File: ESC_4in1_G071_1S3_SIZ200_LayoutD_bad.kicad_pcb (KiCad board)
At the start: 4 copper layers, 26 x 27 mm, 176 parts, among them J1 Conn_01x08, U1 STM32G071GBU6, U10 NCP81161MNTBG, U11 SIZ200DT-T1-GE3, U12 NCP81161MNTBG, U13 SIZ200DT-T1-GE3, U14 TPS630701, U15 TPS72733DSE, U16 INA185, U17 STM32G071GBU6, U18 NCP81161MNTBG, U19 SIZ200DT-T1-GE3, U2 NCP81161MNTBG, U20 NCP81161MNTBG, U21 STM32G071GBU6, U22 SIZ200DT-T1-GE3, U23 NCP81161MNTBG, U24 SIZ200DT-T1-GE3, U25 NCP81161MNTBG, U26 SIZ200DT-T1-GE3, U27 NCP81161MNTBG, U28 STM32G071GBU6, U29 SIZ200DT-T1-GE3, U3 SIZ200DT-T1-GE3, U30 NCP81161MNTBG, U31 SIZ200DT-T1-GE3, U4 NCP81161MNTBG, U5 SIZ200DT-T1-GE3, U6 NCP81161MNTBG, U7 SIZ200DT-T1-GE3, U8 NCP81161MNTBG, U9 SIZ200DT-T1-GE3

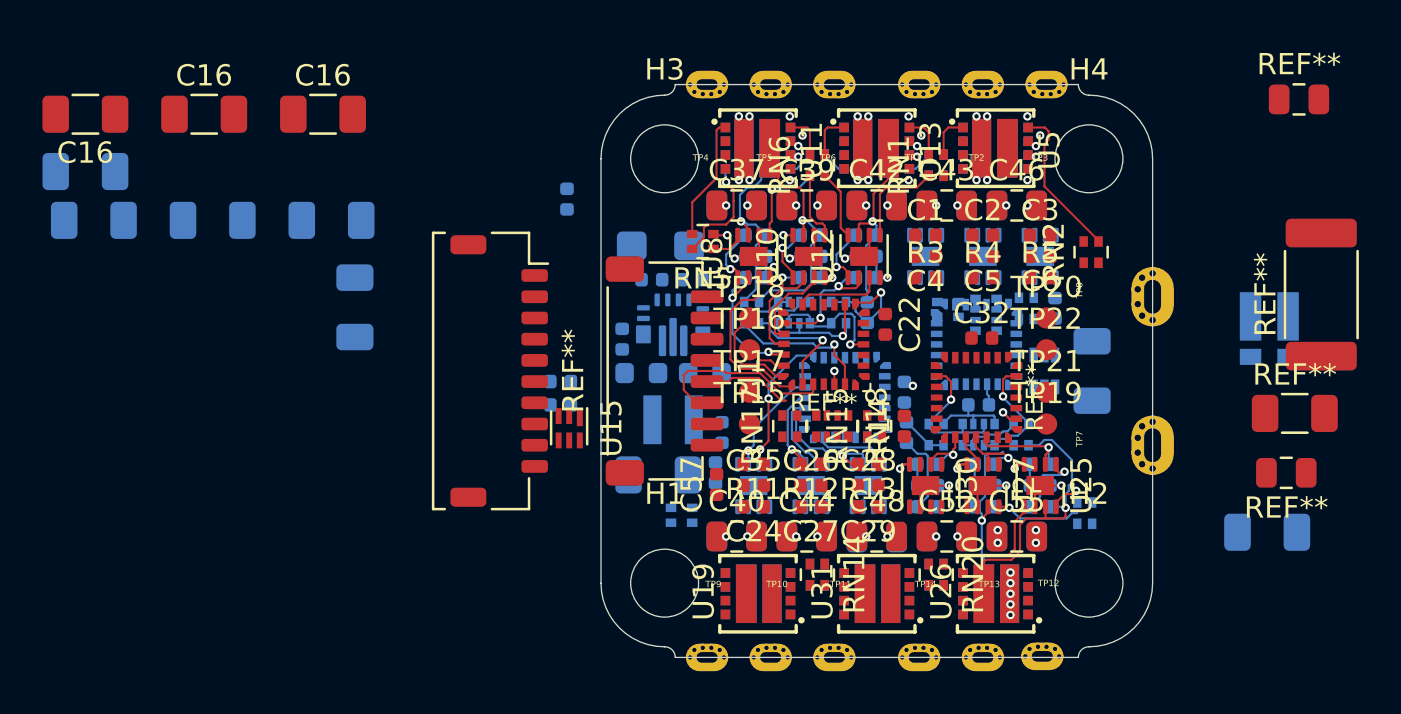
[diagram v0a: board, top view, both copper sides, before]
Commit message: update schematic and layout
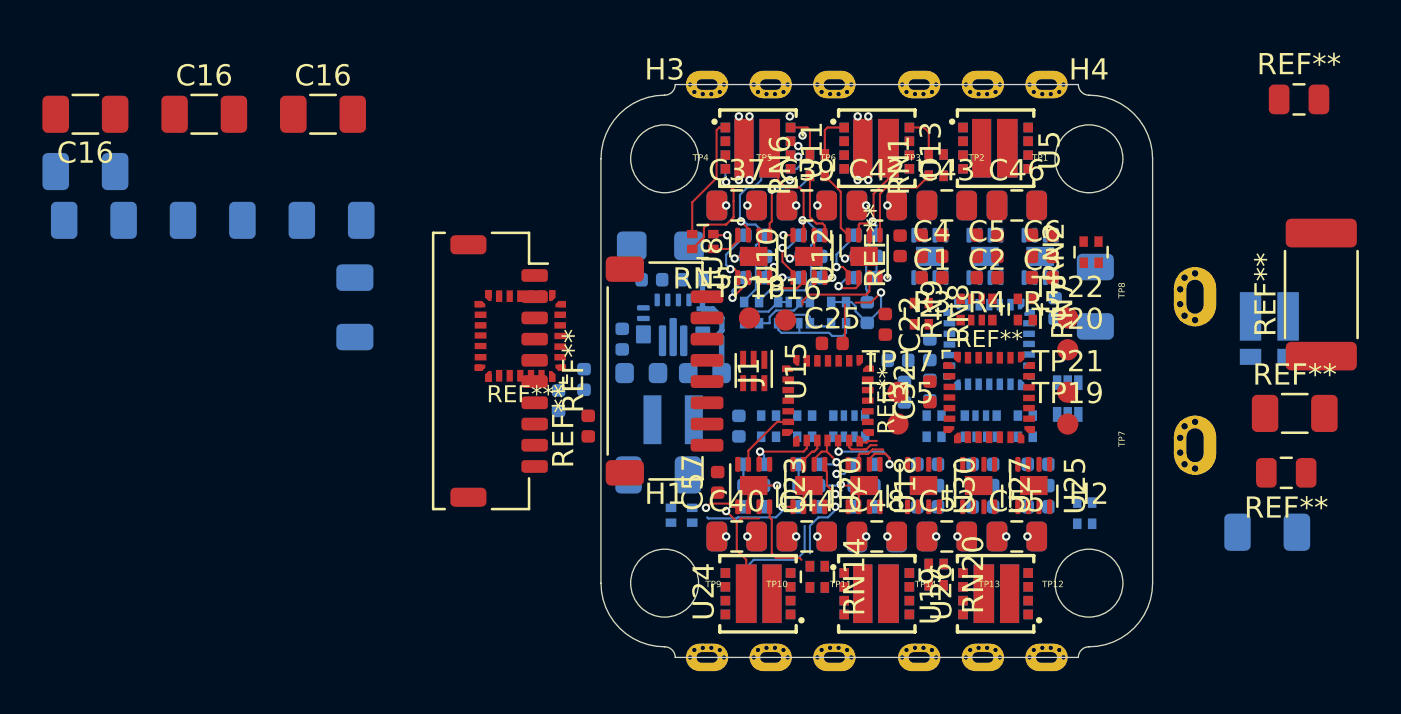
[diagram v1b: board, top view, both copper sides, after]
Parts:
- added REF**: C_0402_1005Metric, Capacitor_SMD:C_0402_1005Metric, F.Cu at (122.4, 77.6)
- C24, C26, C27, C28, C29, C35, R11, R12, R13, R14, RN15, RN17, RN18, U31: moved to B.Cu
- C25, REF**, RN7, RN8, RN9, U18, U20, U21, U23, U24: moved to F.Cu
- moved C18 16.2 mm to (137.3, 76.0), turned to 90 degrees
- moved C19 15.9 mm to (137.0, 74.5)
- moved REF** 15.9 mm to (137.1, 69.1), turned to 90 degrees
- moved U17 14.3 mm to (119.2, 73.3)
- moved U15 9.11 mm to (130.2, 75.0)
- moved C20 8.14 mm to (121.0, 76.4)
- moved R14 7.80 mm to (129.5, 77.6)
- moved TP15 7.00 mm to (137.0, 77.5)
- moved TP17 7.00 mm to (137.0, 76.0)
- moved R2 6.96 mm to (122.2, 75.4), turned to 270 degrees
- moved TP1 6.00 mm to (144.0, 61.5)
- moved TP3 6.00 mm to (138.0, 61.5)
- moved U19 5.60 mm to (136.0, 85.5), turned to 270 degrees
- moved U24 5.60 mm to (130.4, 85.5), turned to 90 degrees
- moved U3 5.60 mm to (141.6, 64.5)
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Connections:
- RN21 pad 1: /ESC3_A -> /ESC3_B
- RN21 pad 2: /ESC3_B -> /ESC3_A
- RN21 pad 3: /ESC3_MB -> /ESC3_MA
- RN21 pad 4: /ESC3_MA -> /ESC3_MB
- U28 pad 14: Net-(U28-Pad14) -> /ESC3_B_EN
- U28 pad 15: Net-(U28-Pad15) -> /ESC3_A_EN
- U28 pad 17: /ESC3_B_EN -> Net-(U28-Pad17)
- U28 pad 22: /ESC3_A_EN -> Net-(U28-Pad22)
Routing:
- net /ESC3_A: track 13.6 -> 0.00 mm, vias 1 -> 0
- net /ESC2_IN: track 9.07 -> 0.00 mm
- net /ESC3_B: track 8.59 -> 0.00 mm, vias 1 -> 0
- net GND: track 26.2 -> 17.9 mm, vias 33 -> 18
- net /ESC2_A_EN: track 8.16 -> 0.00 mm
- net /ESC1_B_GL: track 7.33 -> 0.00 mm
- net /ESC2_MA: track 9.44 -> 2.54 mm, vias 1 -> 0
- net /ESC3_Y: track 6.84 -> 0.00 mm, vias 1 -> 0
- net /ESC4_C: track 0.00 -> 6.32 mm, vias 0 -> 1
- net Net-(C15-Pad2): track 0.00 -> 6.09 mm
- net /ESC3_MA: track 5.86 -> 0.00 mm, vias 1 -> 0
- net /ESC4_B: track 0.00 -> 5.51 mm
- net /ESC2_MB: track 8.50 -> 3.08 mm, vias 1 -> 0
- net /ESC3_A_PWM: track 5.02 -> 0.00 mm, vias 1 -> 0
- net /ESC4_A_EN: track 6.64 -> 1.70 mm, vias 2 -> 0
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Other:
- board text removed: "LAYOUT C"
